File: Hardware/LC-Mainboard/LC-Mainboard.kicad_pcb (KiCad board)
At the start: 2 copper layers, 103 x 63 mm, 2 parts, among them J1 Raspberry_Pi, J2 Charge Controller

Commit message: Update all
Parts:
- added U1: MAX3232IDW, KenwoodFox:MAX3232IDW, F.Cu at (176.0, 86.0)
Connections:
- J2 pad 1: unconnected-(J2-Pad1) -> REN_TX
- J2 pad 2: unconnected-(J2-Pad2) -> REN_RX
- J2 pad 3: unconnected-(J2-Pad3) -> GND

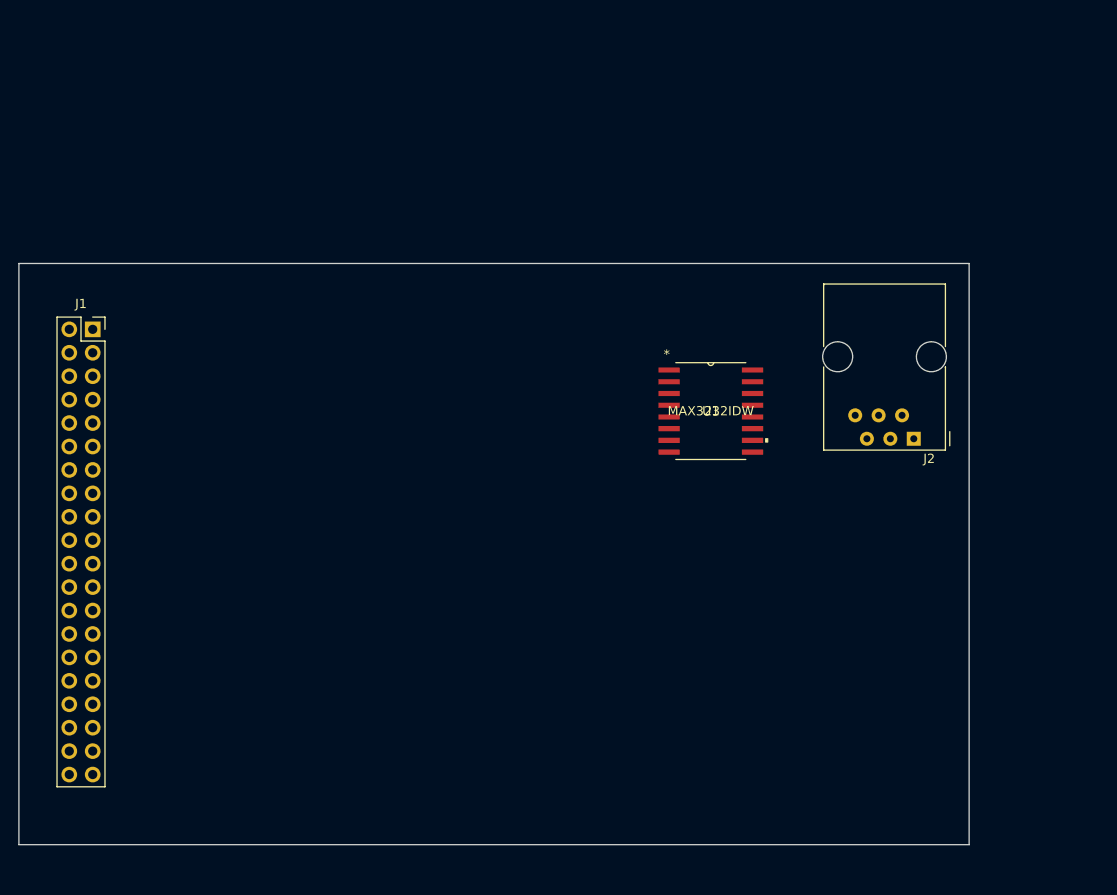
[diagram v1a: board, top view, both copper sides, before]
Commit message: Fix encoder spacer, bump lib and implement max3232 in sch
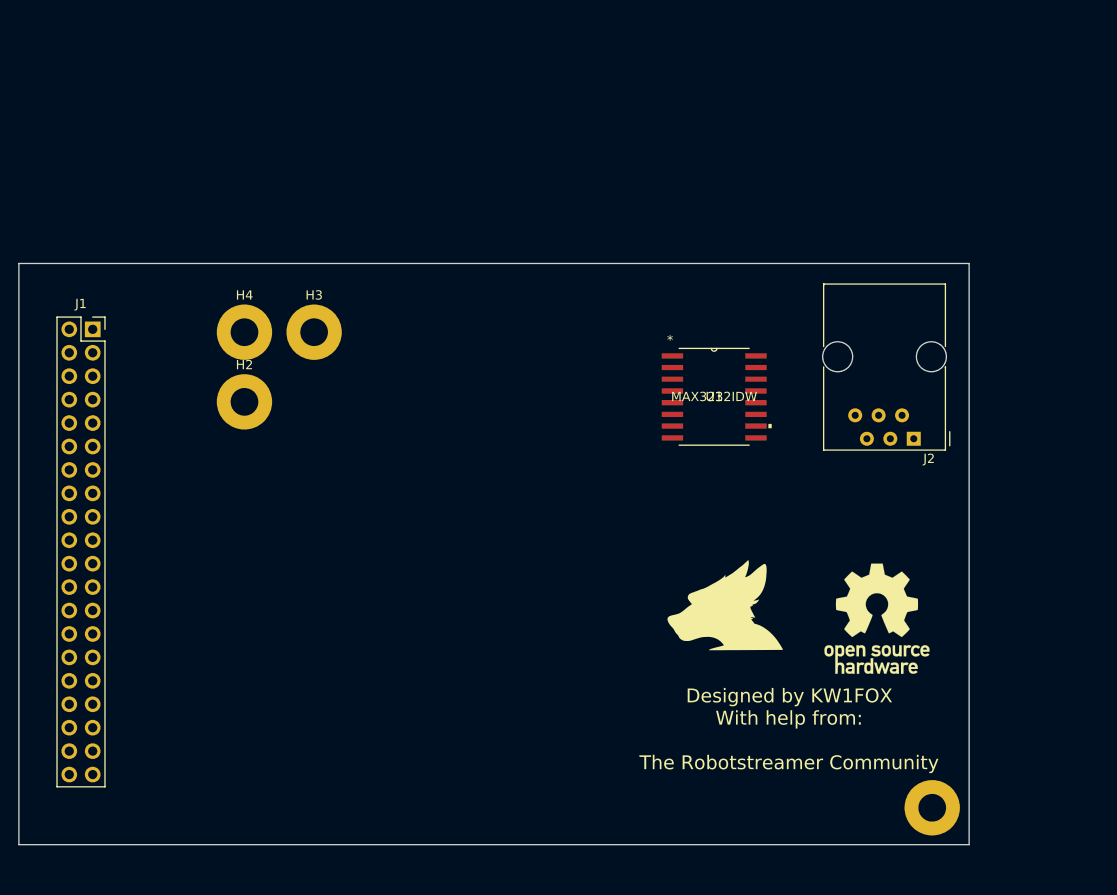
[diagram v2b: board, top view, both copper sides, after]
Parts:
- added G***: LOGO, KenwoodFox:KITSUNE_LOGO, F.Cu at (177.5, 107.0)
- added H1: M_Hole, MountingHole:MountingHole_3mm_Pad, F.Cu at (200.0, 129.0)
- added H2: M_Hole, MountingHole:MountingHole_3mm_Pad, F.Cu at (125.5, 85.0)
- added H3: M_Hole, MountingHole:MountingHole_3mm_Pad, F.Cu at (133.0, 77.5)
- added H4: M_Hole, MountingHole:MountingHole_3mm_Pad, F.Cu at (125.5, 77.5)
- added REF**: OSHW-Logo_11.4x12mm_SilkScreen, Symbol:OSHW-Logo_11.4x12mm_SilkScreen, F.Cu at (194.0, 108.5)
- moved U1 1.59 mm to (176.4, 84.5)
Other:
- board text added: "Designed by KW1FOX With help from: The Robotstreamer Community"

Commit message: Bump
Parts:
- added C1: 0.1μf, Capacitor_SMD:C_0805_2012Metric, F.Cu at (191.5, 106.5)
- added C2: 0.1μf, Capacitor_SMD:C_0805_2012Metric, F.Cu at (193.5, 106.5)
- added C3: 0.1μf, Capacitor_SMD:C_0805_2012Metric, F.Cu at (195.5, 106.5)
- added C4: 0.1μf, Capacitor_SMD:C_0805_2012Metric, F.Cu at (197.5, 106.5)
- added D1: SLR_RX, LED_SMD:LED_0805_2012Metric, F.Cu at (181.5, 97.0)
- added D2: SLR_TX, LED_SMD:LED_0805_2012Metric, F.Cu at (181.5, 94.5)
- added R1: 100k, Resistor_SMD:R_0805_2012Metric, F.Cu at (185.0, 97.0)
- added R2: 100k, Resistor_SMD:R_0805_2012Metric, F.Cu at (185.0, 94.5)
- moved U1 22.8 mm to (195.0, 97.5), turned to 90 degrees
- moved G*** 14.4 mm to (164.0, 112.0)
- moved REF** 14.4 mm to (180.5, 113.5)
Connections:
- J1 pad 1: unconnected-(J1-Pad1) -> +3V3
- J1 pad 10: unconnected-(J1-Pad10) -> PI_RX
- J1 pad 14: unconnected-(J1-Pad14) -> GND
- J1 pad 17: unconnected-(J1-Pad17) -> +3V3
- J1 pad 2: unconnected-(J1-Pad2) -> +5V
- J1 pad 20: unconnected-(J1-Pad20) -> GND
- J1 pad 25: unconnected-(J1-Pad25) -> GND
- J1 pad 30: unconnected-(J1-Pad30) -> GND
- J1 pad 34: unconnected-(J1-Pad34) -> GND
- J1 pad 39: unconnected-(J1-Pad39) -> GND
- J1 pad 4: unconnected-(J1-Pad4) -> +5V
- J1 pad 6: unconnected-(J1-Pad6) -> GND
- J1 pad 8: unconnected-(J1-Pad8) -> PI_TX
- J1 pad 9: unconnected-(J1-Pad9) -> GND
- U1 pad 1: unconnected-(U1-Pad1) -> Net-(U1-Pad1)
- U1 pad 11: unconnected-(U1-Pad11) -> PI_TX
- U1 pad 12: unconnected-(U1-Pad12) -> PI_RX
- U1 pad 13: unconnected-(U1-Pad13) -> REN_TX
- U1 pad 14: unconnected-(U1-Pad14) -> REN_RX
- U1 pad 15: unconnected-(U1-Pad15) -> GND
- U1 pad 16: unconnected-(U1-Pad16) -> +3V3
- U1 pad 2: unconnected-(U1-Pad2) -> Net-(U1-Pad2)
- U1 pad 3: unconnected-(U1-Pad3) -> Net-(U1-Pad3)
- U1 pad 4: unconnected-(U1-Pad4) -> Net-(U1-Pad4)
- U1 pad 5: unconnected-(U1-Pad5) -> Net-(U1-Pad5)
- U1 pad 6: unconnected-(U1-Pad6) -> Net-(U1-Pad6)

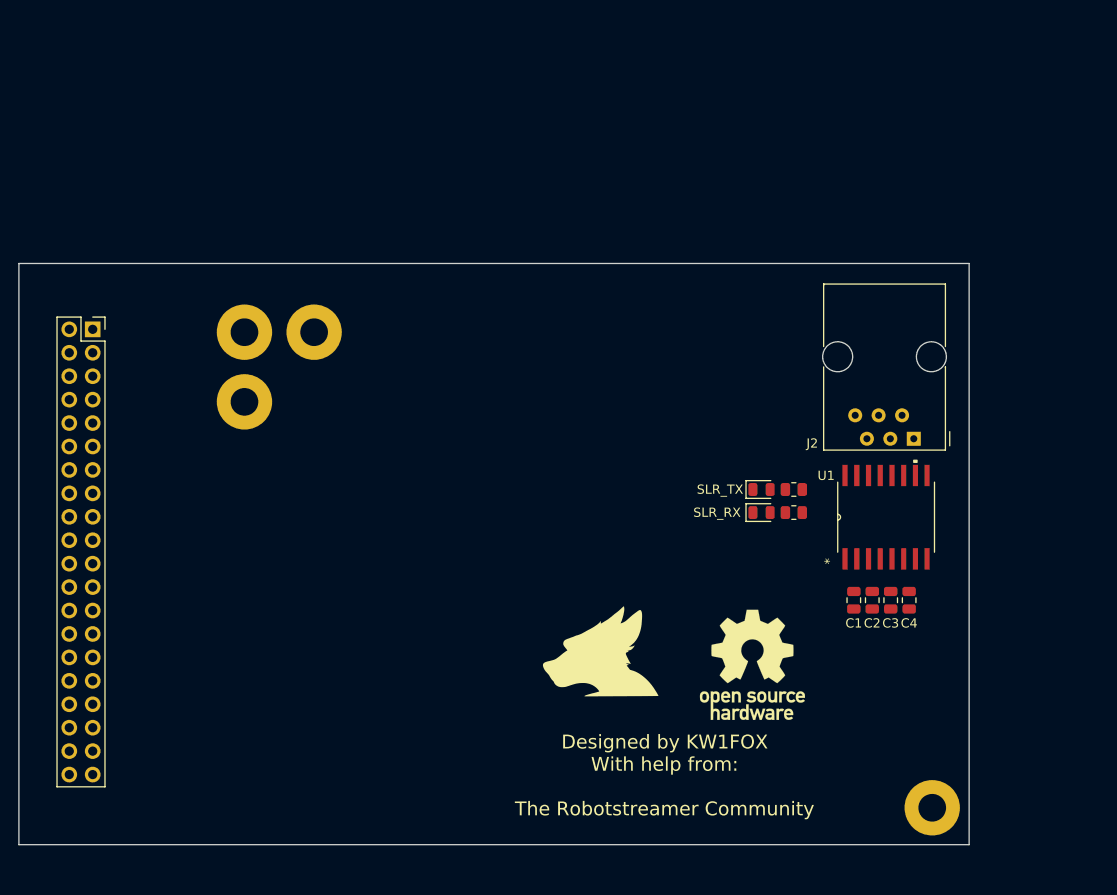
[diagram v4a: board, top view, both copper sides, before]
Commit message: bump lib and add LEDs
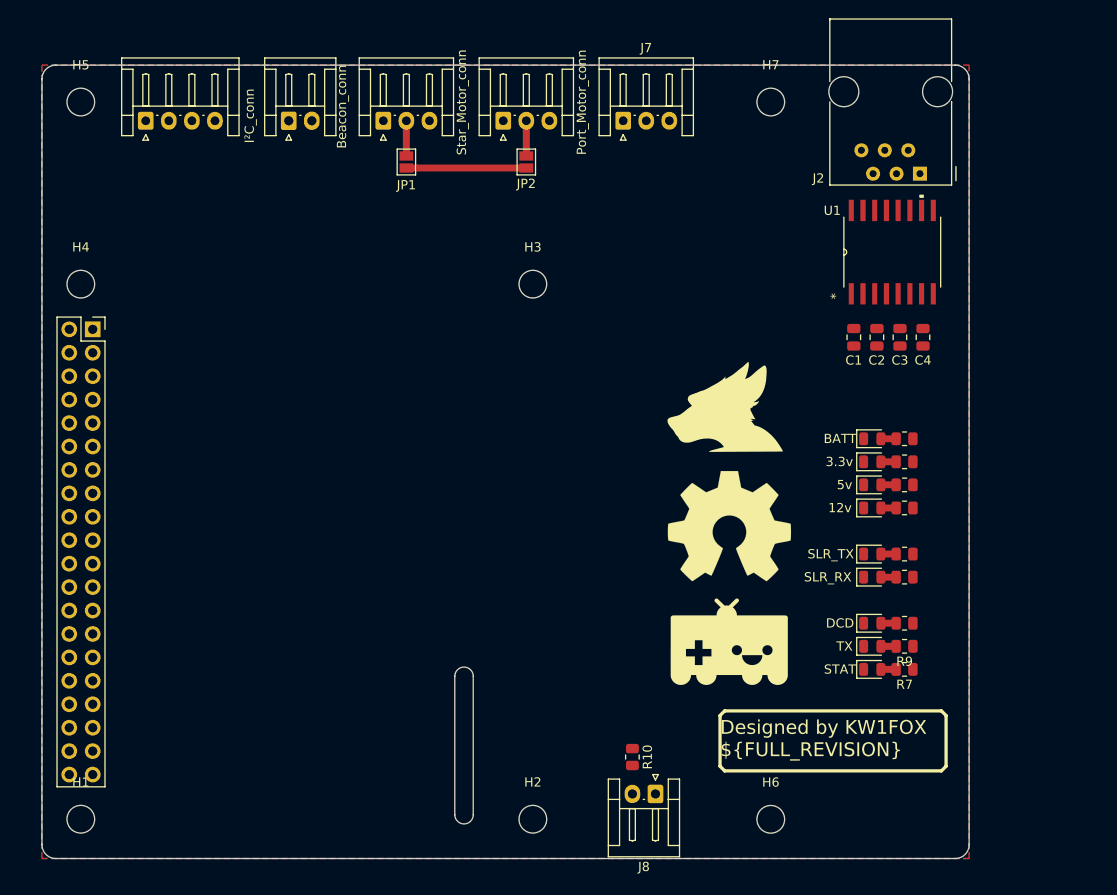
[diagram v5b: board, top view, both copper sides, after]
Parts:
- removed the REF** at (180.5, 113.5)
- added D3: 12v, LED_SMD:LED_0805_2012Metric, F.Cu at (193.5, 96.5)
- added D4: 5v, LED_SMD:LED_0805_2012Metric, F.Cu at (193.5, 94.0)
- added D5: 3.3v, LED_SMD:LED_0805_2012Metric, F.Cu at (193.5, 91.5)
- added D6: DCD, LED_SMD:LED_0805_2012Metric, F.Cu at (193.5, 109.0)
- added D7: STAT, LED_SMD:LED_0805_2012Metric, F.Cu at (193.5, 114.0)
- added D8: BATT, LED_SMD:LED_0805_2012Metric, F.Cu at (193.5, 89.0)
- added D9: TX, LED_SMD:LED_0805_2012Metric, F.Cu at (193.5, 111.5)
- added G***: LOGO, KenwoodFox:ROBOTSTREAMER_LOGO, F.Cu at (178.0, 111.0)
- added H5: BrdMountingHole, MountingHole:MountingHole_3mm, F.Cu at (107.7, 52.5)
- added H6: BrdMountingHole, MountingHole:MountingHole_3mm, F.Cu at (182.5, 130.2)
- added H7: BrdMountingHole, MountingHole:MountingHole_3mm, F.Cu at (182.5, 52.5)
- added J3: I²C_conn, Connector_JST:JST_EH_S4B-EH_1x04_P2.50mm_Horizontal, F.Cu at (114.8, 54.5)
- added J4: Beacon_conn, Connector_JST:JST_EH_S2B-EH_1x02_P2.50mm_Horizontal, F.Cu at (130.2, 54.5)
- added J5: Star_Motor_conn, Connector_JST:JST_EH_S3B-EH_1x03_P2.50mm_Horizontal, F.Cu at (140.5, 54.5)
- added J6: Port_Motor_conn, Connector_JST:JST_EH_S3B-EH_1x03_P2.50mm_Horizontal, F.Cu at (153.5, 54.5)
- added J7: DC_conn, Connector_JST:JST_EH_S3B-EH_1x03_P2.50mm_Horizontal, F.Cu at (166.5, 54.5)
- added J8: PTT_conn, Connector_JST:JST_EH_S2B-EH_1x02_P2.50mm_Horizontal, F.Cu at (170.0, 127.5)
- added JP1: VRM_JP, Jumper:SolderJumper-2_P1.3mm_Open_Pad1.0x1.5mm, F.Cu at (143.0, 59.0)
- added JP2: VRM_JP, Jumper:SolderJumper-2_P1.3mm_Open_Pad1.0x1.5mm, F.Cu at (156.0, 59.0)
- added R10: math, Resistor_SMD:R_0805_2012Metric, F.Cu at (167.5, 123.5)
- added R3: math, Resistor_SMD:R_0805_2012Metric, F.Cu at (197.0, 96.5)
- added R4: math, Resistor_SMD:R_0805_2012Metric, F.Cu at (197.0, 94.0)
- added R5: 100k, Resistor_SMD:R_0805_2012Metric, F.Cu at (197.0, 91.5)
- added R6: 100k, Resistor_SMD:R_0805_2012Metric, F.Cu at (197.0, 109.0)
- added R7: 100k, Resistor_SMD:R_0805_2012Metric, F.Cu at (197.0, 114.0)
- added R8: math, Resistor_SMD:R_0805_2012Metric, F.Cu at (197.0, 89.0)
- added R9: 100k, Resistor_SMD:R_0805_2012Metric, F.Cu at (197.0, 111.5)
- added REF**: OSHW-Symbol_13.4x12mm_SilkScreen, Symbol:OSHW-Symbol_13.4x12mm_SilkScreen, F.Cu at (178.0, 98.5)
- H1, H2, H3, H4: value M_Hole -> PiMountingHole; footprint MountingHole:MountingHole_3mm_Pad -> MountingHole:MountingHole_3mm
- moved H1 92.3 mm to (107.7, 130.2)
- moved H2 55.0 mm to (156.7, 130.2)
- moved G*** 29.7 mm to (177.5, 85.5)
- moved U1 28.7 mm to (195.7, 68.8)
- moved J2 28.7 mm to (198.7, 60.3)
- moved C4 28.5 mm to (199.0, 78.0)
- moved C3 28.5 mm to (196.5, 78.0)
- moved C2 28.5 mm to (194.0, 78.0)
- moved C1 28.5 mm to (191.5, 78.0)
- moved H3 24.3 mm to (156.7, 72.2)
- moved H4 18.5 mm to (107.7, 72.2)
- moved D1 13.9 mm to (193.5, 104.0)
- moved D2 13.9 mm to (193.5, 101.5)
- moved R1 13.9 mm to (197.0, 104.0), turned to 180 degrees
- moved R2 13.9 mm to (197.0, 101.5), turned to 180 degrees
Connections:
- J1 pad 18: unconnected-(J1-Pad18) -> DCD_LED
- J1 pad 22: unconnected-(J1-Pad22) -> PTT
- J1 pad 3: unconnected-(J1-Pad3) -> SDA
- J1 pad 32: unconnected-(J1-Pad32) -> PORT_PWM
- J1 pad 33: unconnected-(J1-Pad33) -> STAR_PWM
- J1 pad 40: unconnected-(J1-Pad40) -> STAT_LED
- J1 pad 5: unconnected-(J1-Pad5) -> SCL
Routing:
- net +5V: track 0.00 -> 13.0 mm
- net Net-(J6-Pad2): track 0.00 -> 3.82 mm
- net Net-(J5-Pad2): track 0.00 -> 3.82 mm
- net Net-(D9-Pad2): track 0.00 -> 1.65 mm
- net Net-(D8-Pad2): track 0.00 -> 1.65 mm
- net Net-(D7-Pad2): track 0.00 -> 1.65 mm
- net Net-(D6-Pad2): track 0.00 -> 1.65 mm
- net Net-(D5-Pad2): track 0.00 -> 1.65 mm
- net Net-(D4-Pad2): track 0.00 -> 1.65 mm
- net Net-(D3-Pad2): track 0.00 -> 1.65 mm
- net Net-(D2-Pad2): track 0.00 -> 1.65 mm
- net Net-(D1-Pad2): track 0.00 -> 1.65 mm
- added copper zone on B.Cu, net GND
- added copper zone on F.Cu, net GND
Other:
- board size 103 x 63 mm -> 100.5 x 86 mm
- board text added: "Designed by KW1FOX ${FULL_REVISION}"
- board text added: "With thanks to Mark Sedutto (KA2QFX) Michael Sedutto TGCFabian And The Robotstreamer Community"
- board text removed: "Designed by KW1FOX With help from: The Robotstreamer Community"

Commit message: Add a bunch of stuff
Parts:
- added J10: Port Enc., Connector_JST:JST_EH_S4B-EH_1x04_P2.50mm_Horizontal, F.Cu at (177.8, 54.5)
- added J9: Star.Enc., Connector_JST:JST_EH_S4B-EH_1x04_P2.50mm_Horizontal, F.Cu at (151.2, 54.5)
- J3: value I²C_conn -> I²C
- J4: value Beacon_conn -> Beacon
- J5: value Star_Motor_conn -> Star.Motor
- J6: value Port_Motor_conn -> Port Motor
- J7: value DC_conn -> DC In
- J8: value PTT_conn -> PTT
- moved J7 57.9 mm to (109.5, 65.0), turned to 90 degrees
- moved H7 16.5 mm to (199.0, 52.5)
- moved D1 15.0 mm to (207.0, 110.5)
- moved D2 15.0 mm to (207.0, 108.0)
- moved D3 15.0 mm to (207.0, 103.0)
- moved D4 15.0 mm to (207.0, 100.5)
- moved D5 15.0 mm to (207.0, 98.0)
- moved D6 15.0 mm to (207.0, 115.5)
- moved D7 15.0 mm to (207.0, 120.5)
- moved D8 15.0 mm to (207.0, 95.5)
- moved D9 15.0 mm to (207.0, 118.0)
- moved G*** 15.0 mm to (191.0, 92.0)
- moved G*** 15.0 mm to (191.5, 117.5)
- moved R1 15.0 mm to (210.5, 110.5)
- moved R2 15.0 mm to (210.5, 108.0)
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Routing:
- net +5V: track 13.0 -> 0.00 mm
- net Net-(J6-Pad2): track 3.82 -> 0.00 mm
- net Net-(J5-Pad2): track 3.82 -> 0.00 mm
- net Net-(D9-Pad2): track 1.65 -> 0.00 mm
- net Net-(D8-Pad2): track 1.65 -> 0.00 mm
- net Net-(D7-Pad2): track 1.65 -> 0.00 mm
- net Net-(D6-Pad2): track 1.65 -> 0.00 mm
- net Net-(D5-Pad2): track 1.65 -> 0.00 mm
- net Net-(D4-Pad2): track 1.65 -> 0.00 mm
- net Net-(D3-Pad2): track 1.65 -> 0.00 mm
- net Net-(D2-Pad2): track 1.65 -> 0.00 mm
- net Net-(D1-Pad2): track 1.65 -> 0.00 mm
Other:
- board size 100.5 x 86 mm -> 114.5 x 86.1 mm
- board text added: "Design by KW1FOX ${FULL_REVISION}"
- board text removed: "Designed by KW1FOX ${FULL_REVISION}"

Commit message: Make a v1.0 hardware release (#2)
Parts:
- removed the H5 at (107.7, 52.5)
- added C5: 10μf, Capacitor_SMD:C_Elec_6.3x5.4, F.Cu at (143.1, 119.0)
- added C6: 0.1μf, Capacitor_SMD:C_0805_2012Metric, F.Cu at (137.3, 116.3)
- added C7: 10μf, Capacitor_SMD:C_Elec_6.3x5.4, F.Cu at (117.5, 108.6)
- added J11: Load En., Connector_JST:JST_XH_S2B-XH-A_1x02_P2.50mm_Horizontal, B.Cu at (135.3, 125.2)
- added Q1: MMBT3906, Package_TO_SOT_SMD:SOT-23, F.Cu at (123.9, 83.4)
- added Q2: MMBT3904, Package_TO_SOT_SMD:SOT-23, F.Cu at (118.9, 87.2)
- added Q3: MMBT3904, Package_TO_SOT_SMD:SOT-23, F.Cu at (122.5, 116.6)
- added R11: 47K, Resistor_SMD:R_0805_2012Metric, F.Cu at (120.9, 83.4)
- added R12: 1K, Resistor_SMD:R_0805_2012Metric, F.Cu at (118.9, 83.4)
- added R13: 47R, Resistor_SMD:R_0805_2012Metric, F.Cu at (127.5, 83.4)
- added R14: 1K, Resistor_SMD:R_0805_2012Metric, F.Cu at (115.3, 88.2)
- added R15: 1K, Resistor_SMD:R_0805_2012Metric, F.Cu at (119.5, 116.6)
- added U2: NCP1117-12_SOT223, Package_TO_SOT_SMD:SOT-223-3_TabPin2, F.Cu at (138.9, 109.8)
- D3: value 12v -> BATT
- D8: value BATT -> LOAD
- J10, J3, J9: footprint Connector_JST:JST_EH_S4B-EH_1x04_P2.50mm_Horizontal -> Connector_JST:JST_XH_S4B-XH-A_1x04_P2.50mm_Horizontal; moved to B.Cu
- J2: moved to B.Cu
- J4, J8: footprint Connector_JST:JST_EH_S2B-EH_1x02_P2.50mm_Horizontal -> Connector_JST:JST_XH_S2B-XH-A_1x02_P2.50mm_Horizontal; moved to B.Cu
- J5, J6: footprint Connector_JST:JST_EH_S3B-EH_1x03_P2.50mm_Horizontal -> Connector_JST:JST_XH_S3B-XH-A_1x03_P2.50mm_Horizontal; moved to B.Cu
- J7: footprint Connector_JST:JST_EH_S3B-EH_1x03_P2.50mm_Horizontal -> Connector_JST:JST_XH_S2B-XH-A_1x02_P2.50mm_Horizontal; moved to B.Cu
- R1, R2, R5, R6, R7, R9: value 100k -> 100R
- R10: value math -> 470R
- R3, R8: value math -> 1K
- R4: value math -> 220R
- moved U1 92.6 mm to (122.0, 98.5), turned to 180 degrees
- moved C4 83.7 mm to (131.2, 95.2), turned to 0 degrees
- moved C3 81.7 mm to (131.2, 97.7), turned to 180 degrees
- moved C2 79.9 mm to (131.2, 100.2), turned to 180 degrees
- moved C1 78.3 mm to (131.2, 102.7), turned to 180 degrees
- moved J7 69.5 mm to (144.3, 125.2), turned to 180 degrees
- moved J2 68.2 mm to (147.7, 78.2)
- moved J5 66.2 mm to (160.0, 117.8), turned to -90 degrees
- moved JP1 59.6 mm to (153.8, 120.2), turned to 180 degrees
- moved J8 52.3 mm to (117.8, 125.0)
- moved R10 52.3 mm to (115.3, 120.4)
- moved J9 50.5 mm to (160.0, 104.2), turned to -90 degrees
- moved D1 39.8 mm to (170.8, 94.0)
- moved D2 39.8 mm to (170.8, 91.5)
- moved D3 39.8 mm to (170.8, 86.5)
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- renumbered H7 to H5
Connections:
- C1 pad 1: +3V3 -> Net-(C1-Pad1)
- C1 pad 2: Net-(C1-Pad2) -> GND
- D9 pad 1: TX_LED -> PTT
- J1 pad 21: unconnected-(J1-Pad21) -> LOAD_EN_Pi
- J1 pad 26: unconnected-(J1-Pad26) -> PORT_ENC_B
- J1 pad 29: unconnected-(J1-Pad29) -> STAR_ENC_B
- J1 pad 31: unconnected-(J1-Pad31) -> PORT_ENC_A
- J1 pad 38: unconnected-(J1-Pad38) -> BCON_LED
- J1 pad 7: unconnected-(J1-Pad7) -> STAR_ENC_A
- J4 pad 2: unconnected-(J4-Pad2) -> BCON_LOAD
- R8 pad 1: +12VA -> LOAD_EN
- U1 pad 2: Net-(C1-Pad2) -> Net-(C1-Pad1)
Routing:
- net +5V: track 0.00 -> 166.7 mm, vias 0 -> 3
- net +3V3: track 0.00 -> 154.7 mm, vias 0 -> 2
- net +12V: track 0.00 -> 121.0 mm, vias 0 -> 4
- net PTT: track 0.00 -> 116.7 mm, vias 0 -> 2
- net LOAD_EN: track 0.00 -> 115.9 mm
- net DCD_LED: track 0.00 -> 77.8 mm, vias 0 -> 3
- net STAR_ENC_A: track 0.00 -> 76.0 mm, vias 0 -> 2
- net STAT_LED: track 0.00 -> 75.9 mm, vias 0 -> 1
- net PI_TX: track 0.00 -> 75.8 mm, vias 0 -> 2
- net PORT_ENC_A: track 0.00 -> 75.2 mm, vias 0 -> 2
- net PI_RX: track 0.00 -> 74.1 mm, vias 0 -> 2
- net PORT_ENC_B: track 0.00 -> 73.2 mm, vias 0 -> 4
- net PORT_PWM: track 0.00 -> 61.0 mm
- net STAR_PWM: track 0.00 -> 59.1 mm, vias 0 -> 2
- net STAR_ENC_B: track 0.00 -> 53.0 mm, vias 0 -> 1
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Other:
- board size 114.5 x 86.1 mm -> 88 x 67 mm
- board text added: "5V"
- board text added: "BAT"
- board text added: "ENC.A"
- board text added: "ENC.B"
- board text added: "PWM"
- board text added: "RELAY"
- board text added: "Robot Mainboard ${FULL_REVISION} Design by KW1FOX"
- board text added: "SCL"
- board text added: "SDA"
- board text removed: "Design by KW1FOX ${FULL_REVISION}"
